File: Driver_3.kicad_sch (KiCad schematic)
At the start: 36 parts

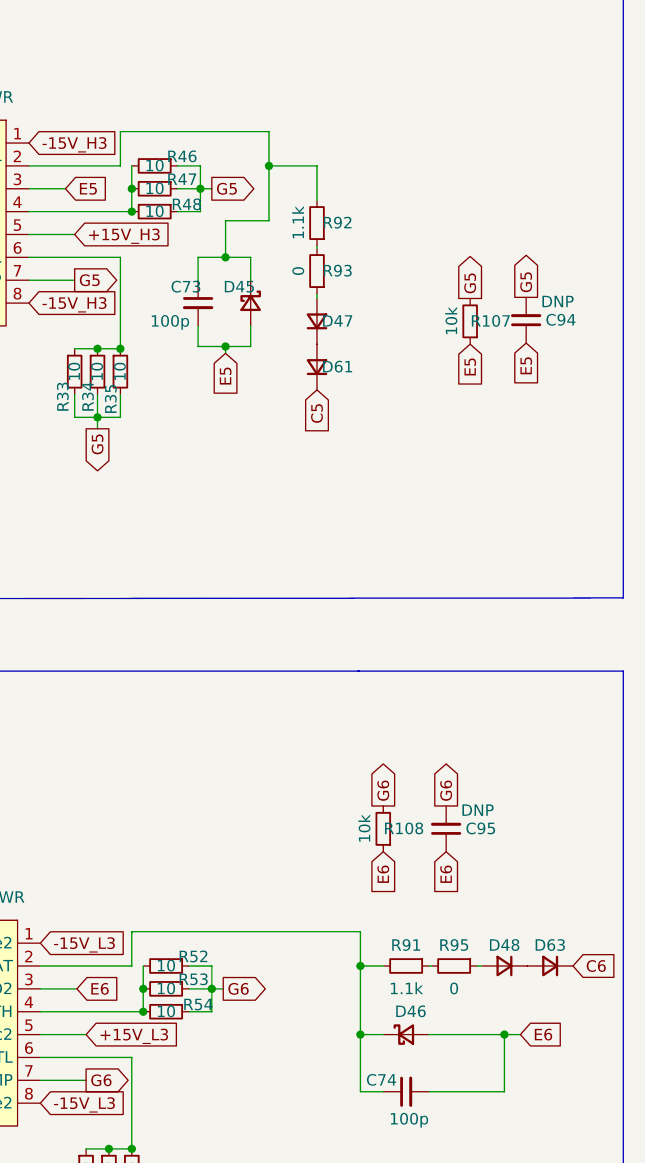
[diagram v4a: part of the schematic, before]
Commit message: VER2.1: переработал цепь DESAT
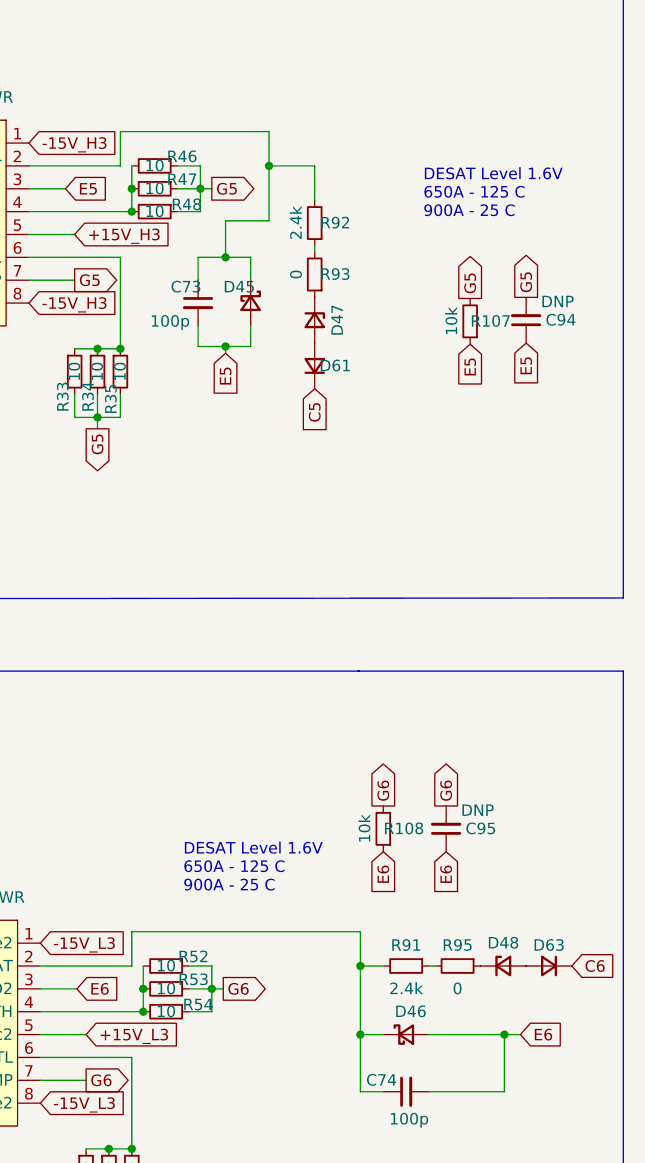
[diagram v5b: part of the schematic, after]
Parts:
- removed D47, D48: MURS160, Diode_SMD:D_SMA_Handsoldering, symbol Device:D_Small
- added D47, D48: MMSZ5232B, Diode_SMD:D_SOD-123, symbol Device:D_Zener_Small
- R91, R92: value 1.1k -> 2.4k
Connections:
- net at D63.2 (A): now also D48.2 (A)
- net at R95.1: now also D48.1 (K)
- net at D61.2 (A): now also D47.2 (A)
- net at R93.1: now also D47.1 (K)
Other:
- note added: "DESAT Level 1.6V 650A - 125 C 900A - 25 C"

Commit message: VER2.1: добавил схему в доки
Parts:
- renumbered D1 to D37, D1 to D44
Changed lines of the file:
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@@
 (kicad_sch
-	(version 20231120)
+	(version 20250114)
 	(generator "eeschema")
-	(generator_version "8.0")
+	(generator_version "9.0")
 	(paper "A4")
+	(text "DESAT Level 1.6V\n650A - 125 C\n900A - 25 C"
+		(exclude_from_sim no)
+		(at 116.205 130.175 0)
+		(effects
+			(font
+				(face "KiCad Font")
+				(size 1.27 1.27)
+			)
+			(justify left)
+		)
+	)
+	(text "Драйвер верхнего ключа"
+		(exclude_from_sim no)
+		(at 71.501 26.543 0)
+		(effects
+			(font
+				(size 1.27 1.27)
+			)
+			(justify left bottom)
+		)
+	)
+	(text "Драйвер нижнего ключа"
+		(exclude_from_sim no)
+		(at 71.247 111.633 0)
+		(effects
+			(font
+				(size 1.27 1.27)
+			)
+			(justify left bottom)
+		)
+	)
+	(text "DESAT Level 1.6V\n650A - 125 C\n900A - 25 C"
+		(exclude_from_sim no)
+		(at 142.875 55.245 0)
+		(effects
+			(font
+				(face "KiCad Font")
+				(size 1.27 1.27)
+			)
+			(justify left)
+		)
+	)
 	(junction
 		(at 107.95 168.91)
@@
 		)
 	)
-	(text "DESAT Level 1.6V\n650A - 125 C\n900A - 25 C"
-		(exclude_from_sim no)
-		(at 116.205 130.175 0)
-		(effects
-			(font
-				(face "KiCad Font")
-				(size 1.27 1.27)
-			)
-			(justify left)
-		)
-	)
-	(text "Драйвер верхнего ключа"
-		(exclude_from_sim no)
-		(at 71.501 26.543 0)
-		(effects
-			(font
-				(size 1.27 1.27)
-			)
-			(justify left bottom)
-		)
-	)
-	(text "Драйвер нижнего ключа"
-		(exclude_from_sim no)
-		(at 71.247 111.633 0)
-		(effects
-			(font
-				(size 1.27 1.27)
-			)
-			(justify left bottom)
-		)
-	)
-	(text "DESAT Level 1.6V\n650A - 125 C\n900A - 25 C"
-		(exclude_from_sim no)
-		(at 142.875 55.245 0)
-		(effects
-			(font
-				(face "KiCad Font")
-				(size 1.27 1.27)
-			)
-			(justify left)
-		)
-	)
 	(global_label "G5"
 		(shape output)
@@
 		(dnp no)
 		(fields_autoplaced yes)
-		(property "Reference" "D1"
+		(property "Reference" "D37"
 			(at 88.9 41.91 0)
 			(effects
@@
 		(dnp no)
 		(fields_autoplaced yes)
-		(property "Reference" "D1"
+		(property "Reference" "D44"
 			(at 90.17 130.81 0)
 			(effects

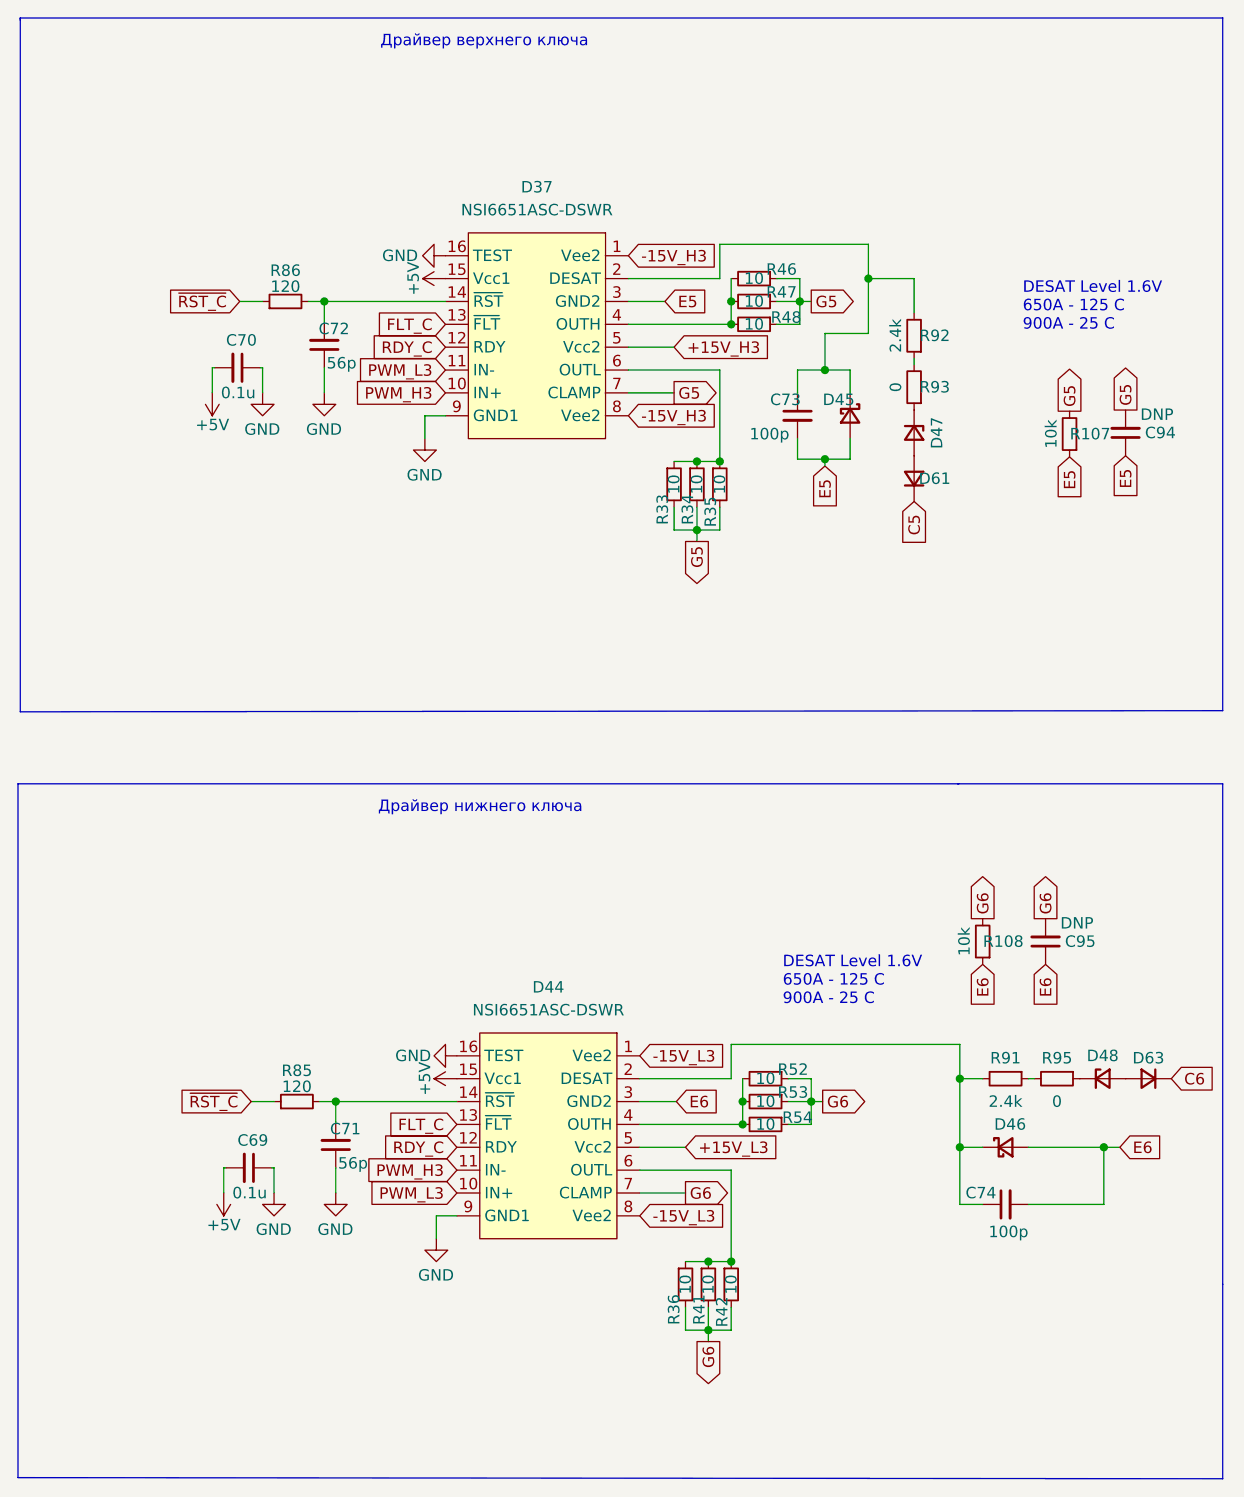
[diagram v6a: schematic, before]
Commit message: VER2.2: удалил лишний затворный резистор
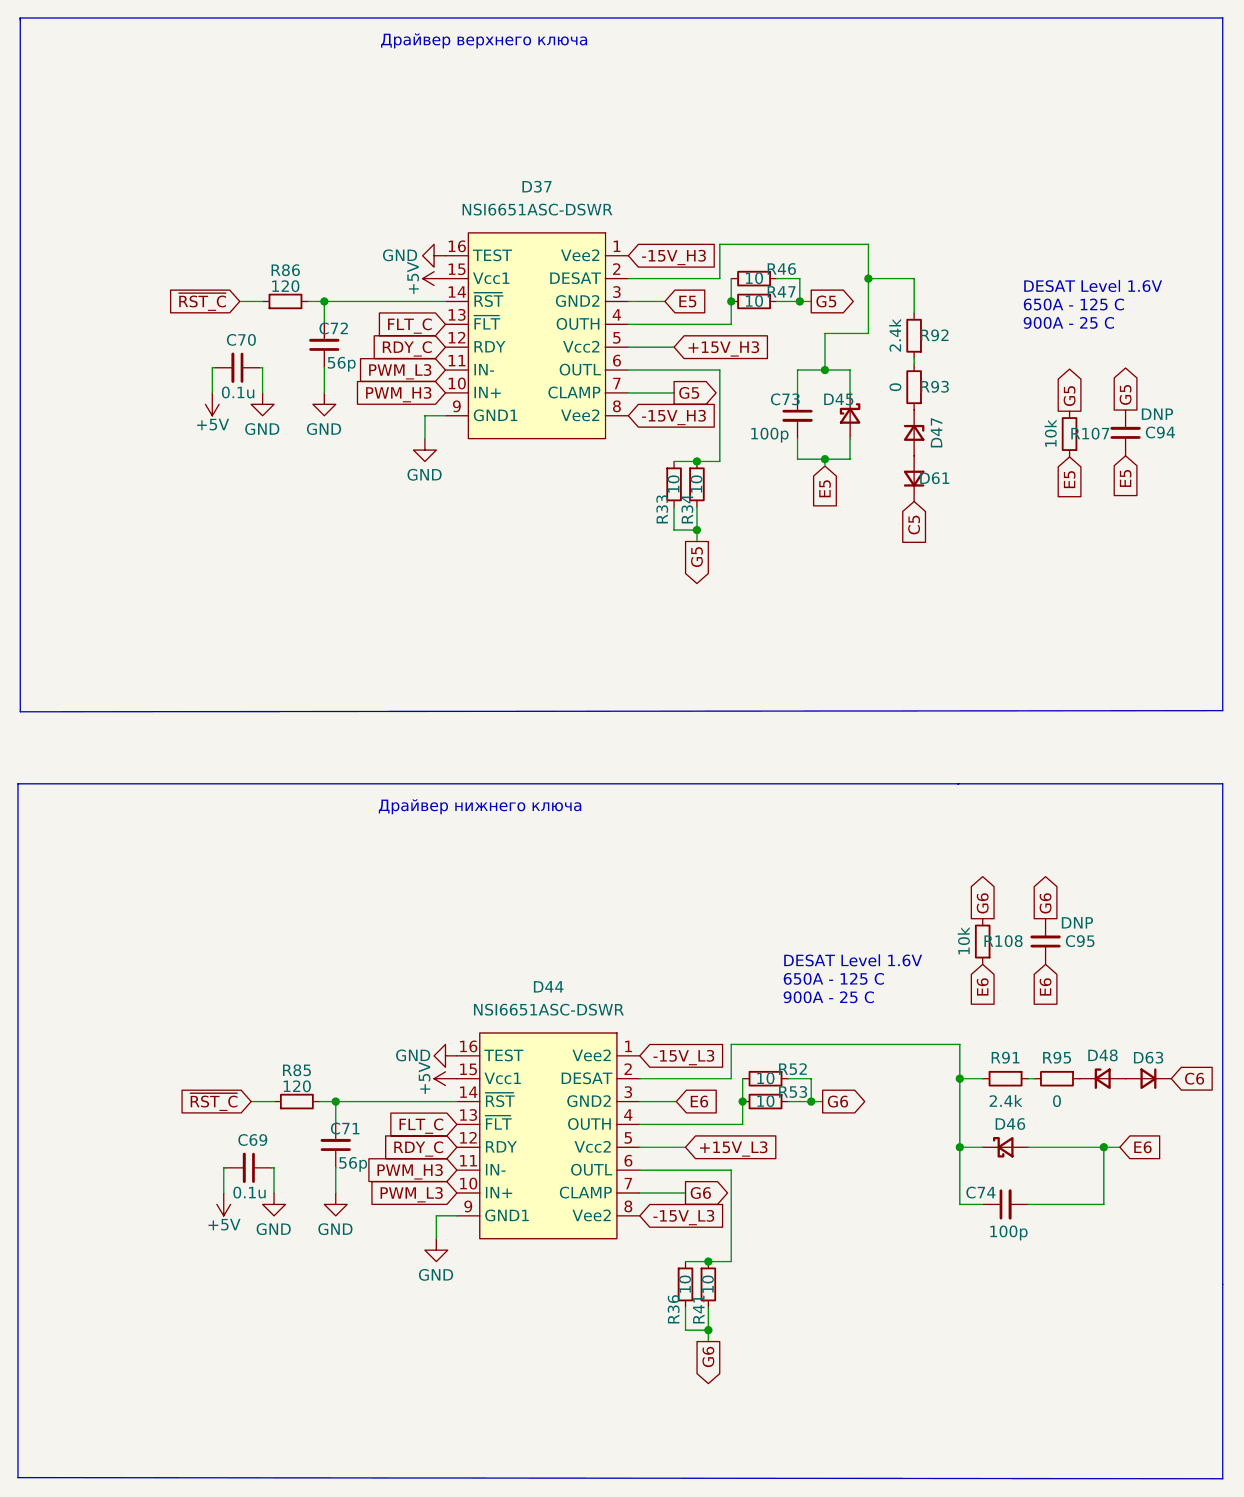
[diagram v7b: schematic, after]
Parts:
- removed R35, R42, R48, R54: 10, Resistor_SMD:R_1206_3216Metric_Pad1.30x1.75mm_HandSolder, symbol Device:R_Small

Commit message: VER2.2: все изменения в списке изменений
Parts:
- D37, D44: value NSI6651ASC-DSWR -> ~; Description P/N (none) -> Gate driver; Product Name (none) -> NSI6651ASC-DSWR
- D45, D46: value MMSZ5240B -> ~; Description P/N (none) -> Zener diode; Product Name (none) -> MMSZ5240B
- D47, D48: value MMSZ5232B -> ~; Description P/N (none) -> Zener diode; Product Name (none) -> MMSZ5232B
- D61, D63: value MURS160 -> ~; Description P/N (none) -> Ultrafast diode; Product Name (none) -> MURS160
